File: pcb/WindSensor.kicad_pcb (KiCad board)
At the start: 2 copper layers, 13 parts, among them P1 SP, P2 0V, P3 3v3, P4 SP, P5 SDA, P6 SCL, P7 5V, P8 GND, P9 GND, U1 ArdinoMinPro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

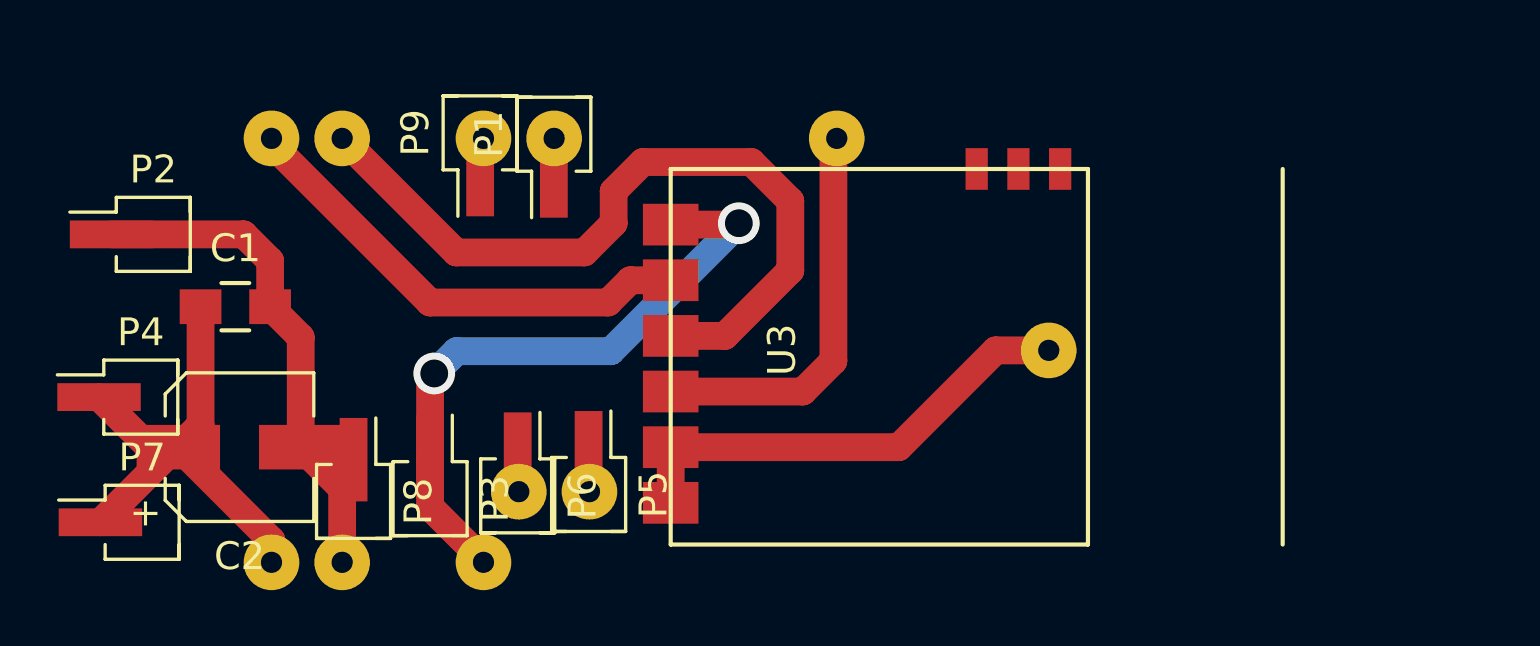
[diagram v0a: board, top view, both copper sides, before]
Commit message: Modularised the libraries and added unit tests, updated pcb, working version
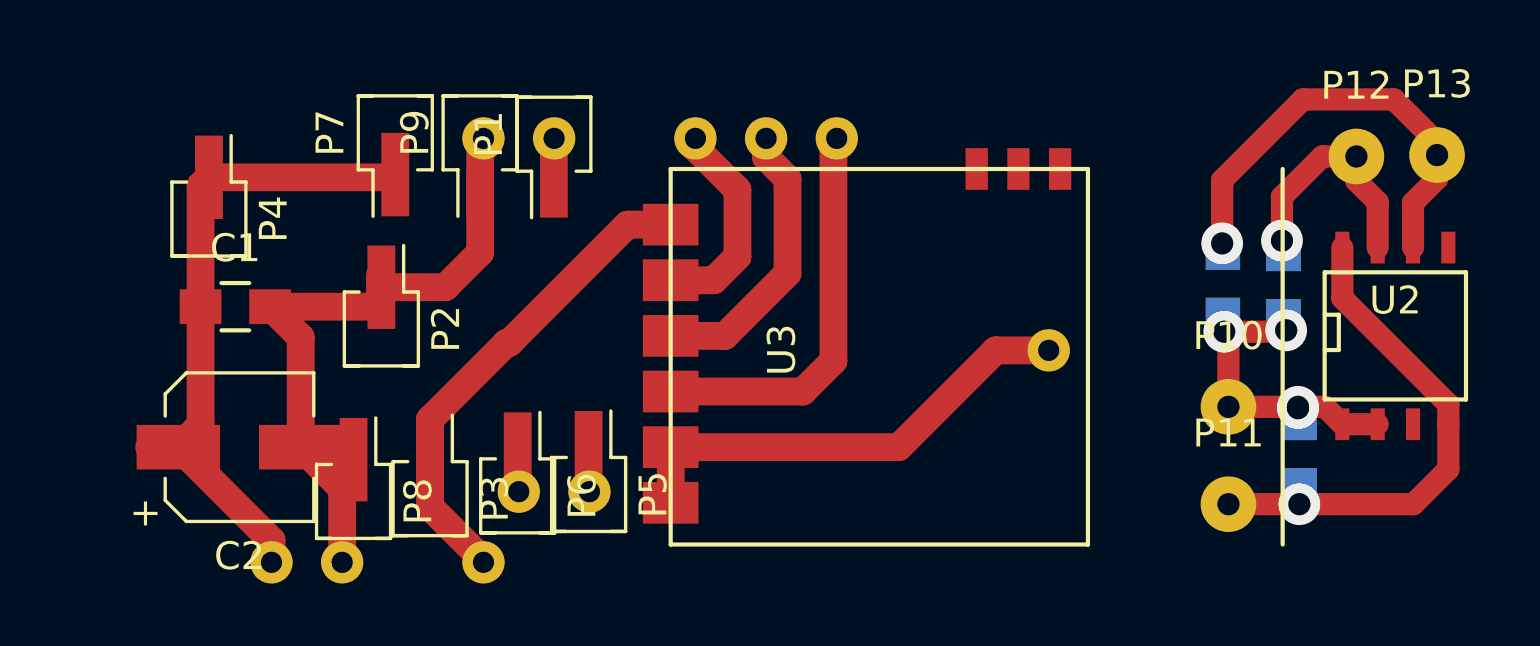
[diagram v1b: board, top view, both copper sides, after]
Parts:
- added C3: 100nF, Capacitors_SMD:C_0805, B.Cu at (153.8, 104.0)
- added P10: 3v3, Wire_Pads:SolderWirePad_single_0-8mmDrill, F.Cu at (151.2, 102.3)
- added P11: GND, Wire_Pads:SolderWirePad_single_0-8mmDrill, F.Cu at (151.2, 105.8)
- added P12: SDA, Wire_Pads:SolderWirePad_single_0-8mmDrill, F.Cu at (155.8, 93.3)
- added P13: SCL, Wire_Pads:SolderWirePad_single_0-8mmDrill, F.Cu at (158.7, 93.2)
- added R1: 4K7, Capacitors_SMD:C_0805, B.Cu at (151.0, 97.9)
- added R2: 4K7, Capacitors_SMD:C_0805, B.Cu at (153.2, 97.9)
- added U2: AS5600, SMD_Packages:SOIC-8-N, F.Cu at (157.2, 99.8)
- moved P7 16.7 mm to (121.2, 92.5), turned to 90 degrees
- moved P2 8.88 mm to (120.8, 99.5), turned to 270 degrees
- moved P4 6.85 mm to (114.5, 95.5), turned to 270 degrees
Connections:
- U1 pad 4: (no net) -> GND
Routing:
- net GND: track 35.0 -> 58.1 mm, vias 0 -> 1
- net RX: track 28.2 -> 10.3 mm
- net SDA: track 0.00 -> 16.4 mm, vias 0 -> 1
- net TX: track 17.2 -> 7.63 mm
- net SCL: track 0.00 -> 9.06 mm, vias 0 -> 1
- net 3v3: track 23.3 -> 30.3 mm, vias 2 -> 4
- net 5V: track 18.4 -> 23.6 mm
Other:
- net class Default: clearance 0.5 -> 0.3; trace_width 1 -> 0.8; via_drill 1 -> 0.8
- rule trace_clearance: 0.5 -> 0.3

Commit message: Switched to 3v hall device, fixed speed sensor to deal with pulse width variations
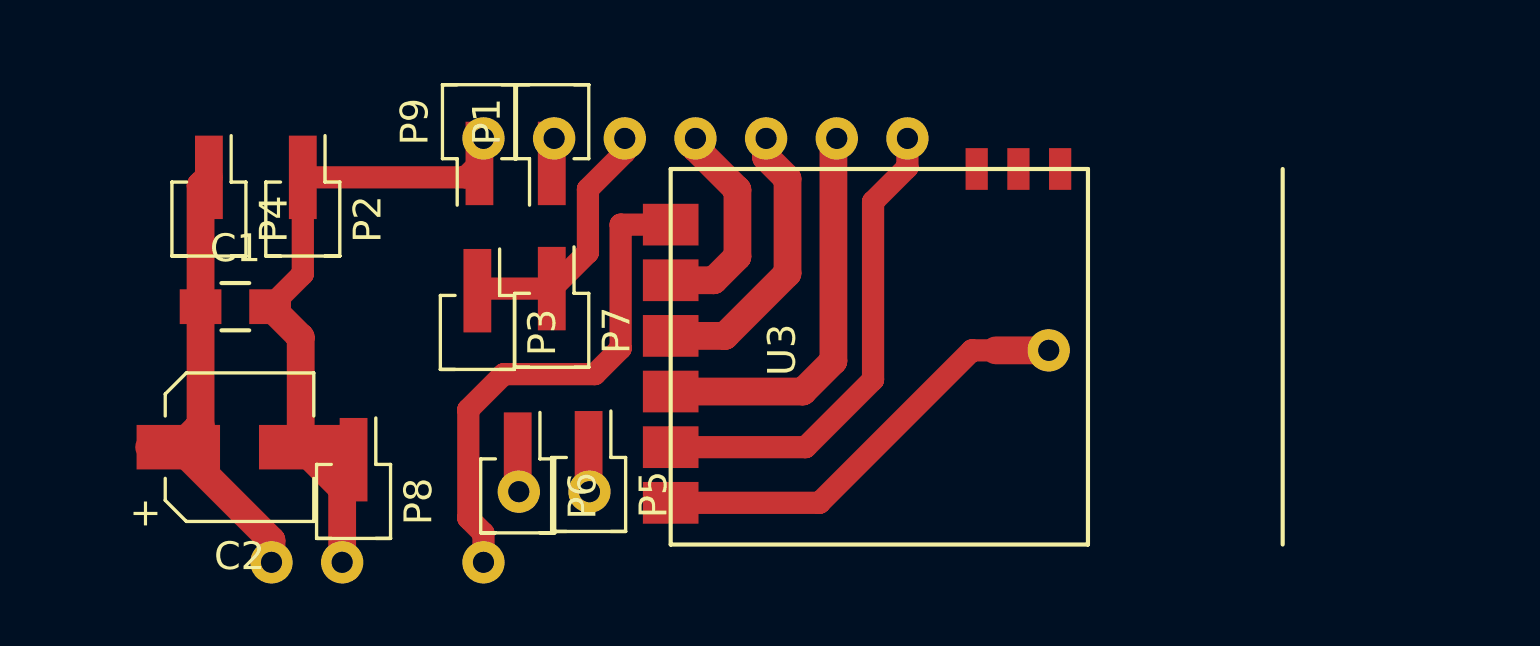
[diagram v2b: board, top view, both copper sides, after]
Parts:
- removed C3: 100nF, Capacitors_SMD:C_0805
- removed P10: 3v3, Wire_Pads:SolderWirePad_single_0-8mmDrill
- removed P11: GND, Wire_Pads:SolderWirePad_single_0-8mmDrill
- removed P12: SDA, Wire_Pads:SolderWirePad_single_0-8mmDrill
- removed P13: SCL, Wire_Pads:SolderWirePad_single_0-8mmDrill
- removed R1, R2: 4K7, Capacitors_SMD:C_0805
- removed U2: AS5600, SMD_Packages:SOIC-8-N
- moved P7 9.06 mm to (126.9, 99.5), turned to 270 degrees
- moved P3 6.21 mm to (124.2, 99.6)
- moved P2 4.86 mm to (117.9, 95.5)
- moved P1 0.46 mm to (126.9, 92.0)
- moved P9 0.40 mm to (124.3, 92.0)
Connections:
- P3 pad 1: 3v3 -> SENSOR_EN
- P7 pad 1: 5V -> SENSOR_EN
- U3 pad 13: GND -> RFEN
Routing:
- net GND: track 58.1 -> 37.8 mm, vias 1 -> 0
- net RFEN: track 0.00 -> 17.5 mm
- net SDA: track 16.4 -> 0.00 mm, vias 1 -> 0
- net 3v3: track 30.3 -> 18.4 mm, vias 4 -> 0
- net SENSOR_EN: track 0.00 -> 9.30 mm
- net SCL: track 9.06 -> 0.00 mm, vias 1 -> 0
- net 5V: track 23.6 -> 16.8 mm
